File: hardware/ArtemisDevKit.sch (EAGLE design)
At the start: 81 parts, among them J2 CORTEX_JTAG_DEBUG_MINIMUM_PTH, J3 CORTEX_JTAG_DEBUG_PTH, J5 1X04_SMD_STRAIGHT_COMBO, J6 QWIIC_RIGHT_ANGLE, J7 CAMERA-HIMAX, J9 1X04_SMD_STRAIGHT_COMBO, U1 DAPLINK_KL26Z, U2 ARTEMIS_MODULESMD, U3 LIS2DH12, U4 AP2127K-1.8V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

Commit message: clean slate for v03
- renamed to ArtemisDevKit
- renamed parts library
- removed old gerber files
- removed old BOM
- added .DS_Store to .gitignore for MacOS
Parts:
- FRAME1: REV v02 -> v03

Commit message: initial changes for v03
- moved Apollo3 reset (TGT_RESET) to TARGET_NRESET on interface chip (pin c1)
- moved TGT_BOOT to pin e30 (pad 9) of the interface chip (still meant to be pulled low most of the time - just making provisions for software control / serial bootloader compatibility later)
- removed test point on clock lines
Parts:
- removed S1: DIP-04SMD, SparkFun-Switches:DIP-04SMD
- removed TP5: TEST-POINT3X5, SparkFun-Connectors:TEST-POINT3X5
- added JP2: JUMPER-SMT_2_NC_TRACE_SILK, SparkFun-Jumpers:JUMPER-SMT_2_NC_TRACE_SILK
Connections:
- net !RST renamed !INTFC_RST
- net TCLK renamed INTFC_SWDCLK
- net TDI renamed INTFC_NC5
- net TDO renamed INTFC_NC6
- net TMS renamed INTFC_SWDIO
- removed net !TGT_RST!_IF: S1.1A, U1.NRESET_FB_ISP
- removed net N$11: JP1.1, U1.WAKE_NREQ
- removed net N$17: S1.3A, U1.TGT_SWDIO
- net !TGT_RST: now also U1.TGT_NRESET; no longer S1.1B
- net N$12: now also JP2.1, U1.TGT_SWCLK; no longer S1.4A, U1.TGT_SWO
- net N$13: no longer TP5.1
- net N$18: now also JP1.1, U1.NC1; no longer S1.2A, U1.TGT_SWCLK
- net TGT_SWCLK: now also JP2.2; no longer S1.2B
- net TGT_SWDIO: now also U1.TGT_SWDIO; no longer S1.3B
- net TGT_SWO: now also U1.TGT_SWO; no longer S1.4B
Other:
- moved on the sheet: J3, JP1

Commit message: board changes to match initial changes
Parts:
- J1: device SparkFun-Connectors:USB_C2-LAYER -> SparkFun-Connectors:USB_C_2-LAYER
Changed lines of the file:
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@@
 <part name="GND11" library="SparkFun-PowerSymbols" deviceset="GND" device=""/>
 <part name="C4" library="SparkFun-Capacitors" deviceset="0.1UF" device="-0603-25V-5%" value="0.1uF"/>
-<part name="TP11" library="SparkFun-Connectors" deviceset="TEST-POINT" device="3X5" value=""/>
+<part name="TP11" library="SparkFun-Connectors" deviceset="TEST-POINT" device="3X5" value="TEST-POINT3X5"/>
 <part name="R12" library="SparkFun-Resistors" deviceset="10KOHM" device="-0603-1/10W-1%" value="10k"/>
-<part name="J1" library="SparkFun-Connectors" deviceset="USB_C" device="2-LAYER"/>
+<part name="J1" library="SparkFun-Connectors" deviceset="USB_C" device="_2-LAYER"/>
 <part name="R6" library="SparkFun-Resistors" deviceset="5.1KOHM" device="5.1KOHM-0603-1/10W-1%" value="5.1k"/>
 <part name="R7" library="SparkFun-Resistors" deviceset="5.1KOHM" device="5.1KOHM-0603-1/10W-1%" value="5.1k"/>
@@
 <part name="GND18" library="SparkFun-PowerSymbols" deviceset="GND" device=""/>
 <part name="GND20" library="SparkFun-PowerSymbols" deviceset="GND" device=""/>
-<part name="TP4" library="SparkFun-Connectors" deviceset="TEST-POINT" device="3X5" value=""/>
-<part name="TP3" library="SparkFun-Connectors" deviceset="TEST-POINT" device="3X5" value=""/>
+<part name="TP4" library="SparkFun-Connectors" deviceset="TEST-POINT" device="3X5" value="TEST-POINT3X5"/>
+<part name="TP3" library="SparkFun-Connectors" deviceset="TEST-POINT" device="3X5" value="TEST-POINT3X5"/>
 <part name="X1" library="SparkFun-Clocks" deviceset="CRYSTAL-16MHZ_SMALL" device="" value="16MHz"/>
 <part name="GND19" library="SparkFun-PowerSymbols" deviceset="GND" device=""/>

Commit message: update labels
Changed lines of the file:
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@@
 <text x="210.82" y="88.9" size="1.778" layer="97" font="vector">I2C Address:
 0x19 (SA0 = 1)</text>
-<wire x1="165.1" y1="279.4" x2="165.1" y2="111.76" width="0.2032" layer="97" style="longdash"/>
-<wire x1="165.1" y1="111.76" x2="165.1" y2="0" width="0.2032" layer="97" style="longdash"/>
-<wire x1="0" y1="111.76" x2="165.1" y2="111.76" width="0.2032" layer="97" style="longdash"/>
-<wire x1="165.1" y1="111.76" x2="330.2" y2="111.76" width="0.2032" layer="97" style="longdash"/>
+<wire x1="162.56" y1="279.4" x2="162.56" y2="111.76" width="0.2032" layer="97" style="longdash"/>
+<wire x1="162.56" y1="111.76" x2="162.56" y2="0" width="0.2032" layer="97" style="longdash"/>
+<wire x1="0" y1="111.76" x2="162.56" y2="111.76" width="0.2032" layer="97" style="longdash"/>
+<wire x1="162.56" y1="111.76" x2="330.2" y2="111.76" width="0.2032" layer="97" style="longdash"/>
 <wire x1="330.2" y1="111.76" x2="330.2" y2="228.6" width="0.2032" layer="97" style="longdash"/>
 <wire x1="330.2" y1="228.6" x2="330.2" y2="279.4" width="0.2032" layer="97" style="longdash"/>
@@
 <instance part="TP4" gate="G$1" x="121.92" y="165.1">
 <attribute name="NAME" x="127" y="165.1" size="1.778" layer="95" font="vector"/>
-<attribute name="VALUE" x="119.38" y="162.56" size="1.778" layer="96" font="vector"/>
 </instance>
 <instance part="TP3" gate="G$1" x="121.92" y="162.56">
 <attribute name="NAME" x="127" y="162.56" size="1.778" layer="95" font="vector"/>
-<attribute name="VALUE" x="119.38" y="160.02" size="1.778" layer="96" font="vector"/>
 </instance>
 <instance part="X1" gate="G$1" x="43.18" y="160.02">

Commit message: connect PTB1 to PTC1
PTB1 (pin 21 on the 32-pin QFN package) is for 'SW_RESET_BUTTON' in the DAPLink firmware - this is for detecting when the user wants to enter DAPLink maintenance mode
PTC1 (pin 22 on the 32-pin package) is meant to actually control the reset line of the Artemis - this was the mistake that was fixed with a green-wire on the v02 prototype.

The effect of this change is that the user can hold the Artemis reset line while plugging in the DK to enter maintenance mode where they can upgrade the interface firmware, and also that the Artemis will be automatically reset when drag+drop programming occurs
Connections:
- net !TGT_RST: now also U1.NRESET_FB_ISP

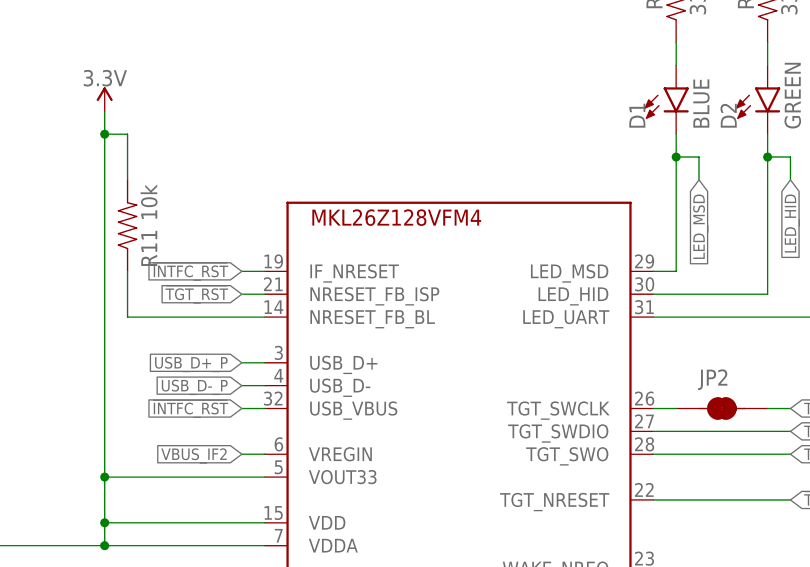
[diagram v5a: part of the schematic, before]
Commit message: final touches for review
- updated library in use for the interface chip
- mitered jumper labels
- approved / fixed all drc errors
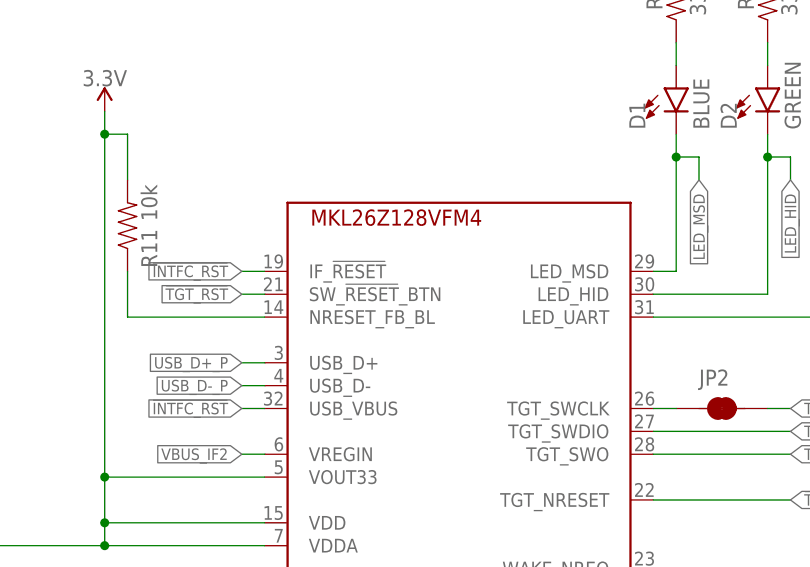
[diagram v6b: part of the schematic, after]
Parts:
- U1: device artembed:DAPLINK_KL26Z -> ArtemisDevKit:DAPLINK_KL26Z
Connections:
- net !INTFC_RST: now also U1.IF_!RESET; no longer U1.IF_NRESET
- net !TGT_RST: now also U1.SW_!RESET!_BTN; no longer U1.NRESET_FB_ISP
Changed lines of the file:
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@@
 <attribute name="REV" value="v03"/>
 </part>
-<part name="U1" library="artembed" deviceset="DAPLINK_KL26Z" device=""/>
+<part name="U1" library="ArtemisDevKit" deviceset="DAPLINK_KL26Z" device=""/>
 <part name="GND11" library="SparkFun-PowerSymbols" deviceset="GND" device=""/>
 <part name="C4" library="SparkFun-Capacitors" deviceset="0.1UF" device="-0603-25V-5%" value="0.1uF"/>
@@
 </segment>
 <segment>
-<pinref part="U1" gate="G$1" pin="IF_NRESET"/>
+<pinref part="U1" gate="G$1" pin="IF_!RESET"/>
 <wire x1="66.04" y1="213.36" x2="68.58" y2="213.36" width="0.1524" layer="91"/>
 <label x="66.04" y="213.36" size="1.27" layer="95" rot="R180" xref="yes"/>
@@
 </segment>
 <segment>
-<pinref part="U1" gate="G$1" pin="NRESET_FB_ISP"/>
+<pinref part="U1" gate="G$1" pin="SW_!RESET!_BTN"/>
 <wire x1="68.58" y1="210.82" x2="66.04" y2="210.82" width="0.1524" layer="91"/>
 <label x="66.04" y="210.82" size="1.27" layer="95" rot="R180" xref="yes"/>

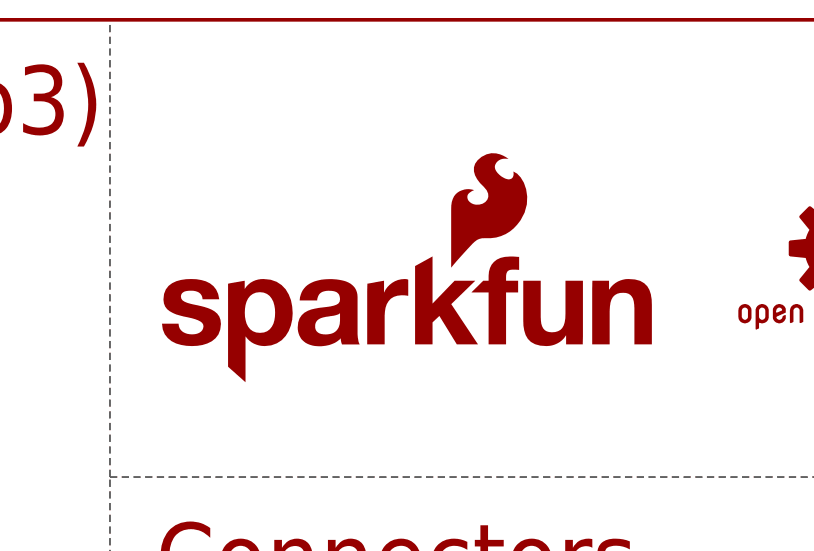
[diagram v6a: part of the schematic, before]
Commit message: remove old buzzard libraries and delete old silk
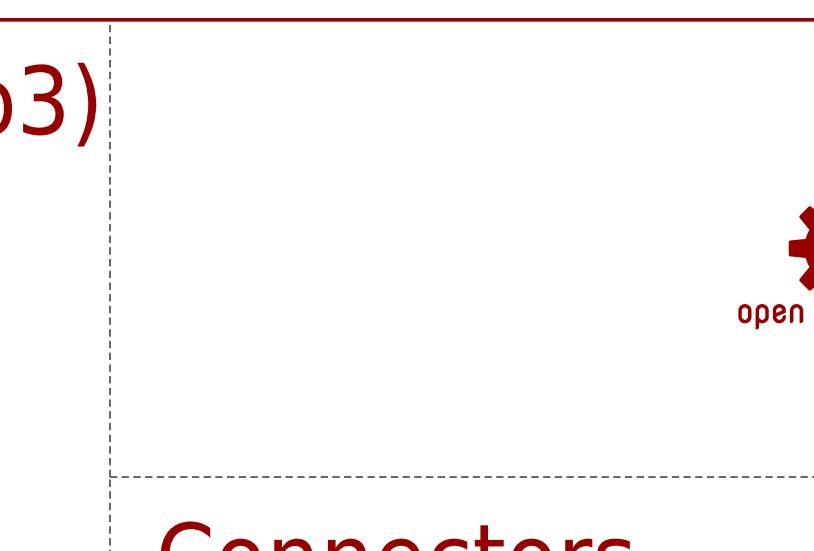
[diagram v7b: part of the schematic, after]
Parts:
- removed LOGO2: SFE_LOGO_NAME_FLAME.2_INCH, SparkFun-Aesthetics:SFE_LOGO_NAME_FLAME.2_INCH
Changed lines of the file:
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@@
 <?xml version="1.0" encoding="utf-8"?>
 <!DOCTYPE eagle SYSTEM "eagle.dtd">
-<eagle version="9.5.2">
+<eagle version="9.6.0">
 <drawing>
 <settings>
@@
 <part name="FD4" library="SparkFun-Aesthetics" deviceset="FIDUCIAL" device="1X2"/>
 <part name="LOGO1" library="SparkFun-Aesthetics" deviceset="OSHW-LOGO" device="S"/>
-<part name="LOGO2" library="SparkFun-Aesthetics" deviceset="SFE_LOGO_NAME_FLAME" device=".2_INCH"/>
 <part name="JP2" library="SparkFun-Jumpers" deviceset="JUMPER-SMT_2_NC_TRACE" device="_SILK" package3d_urn="urn:adsk.eagle:package:39281/1"/>
 </parts>
@@
 <instance part="FD4" gate="G$1" x="429.26" y="30.48" smashed="yes"/>
 <instance part="LOGO1" gate="G$1" x="411.48" y="254" smashed="yes"/>
-<instance part="LOGO2" gate="G$1" x="335.28" y="238.76" smashed="yes"/>
 <instance part="JP2" gate="G$1" x="119.38" y="198.12" smashed="yes">
 <attribute name="NAME" x="116.84" y="200.66" size="1.778" layer="95" font="vector"/>
